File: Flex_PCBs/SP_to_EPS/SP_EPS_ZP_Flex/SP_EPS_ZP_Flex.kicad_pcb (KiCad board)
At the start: 2 copper layers, 4.5 x 55 mm, 2 parts, among them J1 Conn_01x08_Male, J2 Conn_01x08_Male

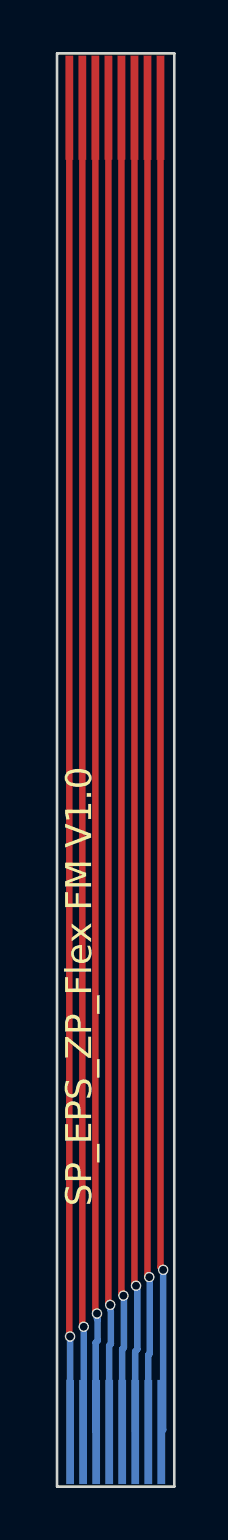
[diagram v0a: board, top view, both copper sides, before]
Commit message: Update the EPS FlexPCBs, with correct top/down and crossed out
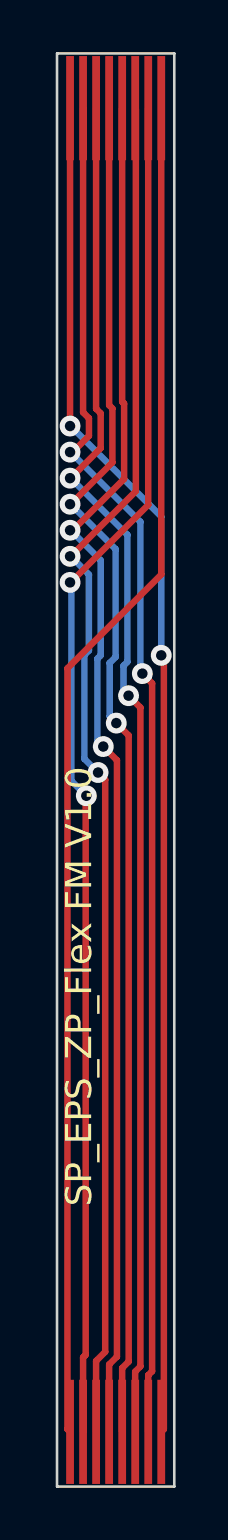
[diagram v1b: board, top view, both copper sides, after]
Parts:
- J2: moved to F.Cu
- moved J2 4.50 mm to (120.0, 109.9), turned to 0 degrees
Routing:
- net 5: track 50.8 -> 52.8 mm, vias 1 -> 2
- net 3: track 50.9 -> 52.7 mm, vias 1 -> 2
- net 6: track 50.9 -> 52.7 mm, vias 1 -> 2
- net 7: track 50.9 -> 52.6 mm, vias 1 -> 2
- net 4: track 51.0 -> 52.7 mm, vias 1 -> 2
- net 8: track 50.8 -> 52.3 mm, vias 1 -> 2
- net 1: track 50.9 -> 52.3 mm, vias 1 -> 0
- net 2: track 51.0 -> 52.4 mm, vias 1 -> 2
